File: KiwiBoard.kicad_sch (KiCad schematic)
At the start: 22 parts, among them J1 12V Power, J1 Motor Connector, J2 Heater, J3 Encoder Connector, J3 Expansion, J3 Fan, J4 OLED, K1 G5LE-14 DC3, Q1 PN2222A, Q3 TIP120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

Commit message: Change to JST PH connectors for OLED and Encoder.  Adjust spacing for the 3v3 regulator
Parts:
- J3: footprint Connector_PinSocket_2.54mm:PinSocket_1x05_P2.54mm_Vertical -> Connector_JST:JST_PH_B5B-PH-K_1x05_P2.00mm_Vertical
- J4: footprint Connector_JST:JST_SH_BM04B-SRSS-TB_1x04-1MP_P1.00mm_Vertical -> Connector_JST:JST_PH_B5B-PH-K_1x05_P2.00mm_Vertical
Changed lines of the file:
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@@
       (effects (font (size 1.27 1.27)) (justify left))
     )
-    (property "Footprint" "Connector_PinSocket_2.54mm:PinSocket_1x05_P2.54mm_Vertical" (at 236.855 93.345 0)
+    (property "Footprint" "Connector_JST:JST_PH_B5B-PH-K_1x05_P2.00mm_Vertical" (at 236.855 93.345 0)
       (effects (font (size 1.27 1.27)) hide)
     )
@@
       (effects (font (size 1.27 1.27)) (justify left))
     )
-    (property "Footprint" "Connector_JST:JST_SH_BM04B-SRSS-TB_1x04-1MP_P1.00mm_Vertical" (at 231.775 73.025 0)
-      (effects (font (size 1.27 1.27)) hide)
-    )
+    (property "Footprint" "Connector_JST:JST_PH_B5B-PH-K_1x05_P2.00mm_Vertical" (at 231.775 73.025 0)
+      (effects (font (size 1.27 1.27)) hide)
+    )

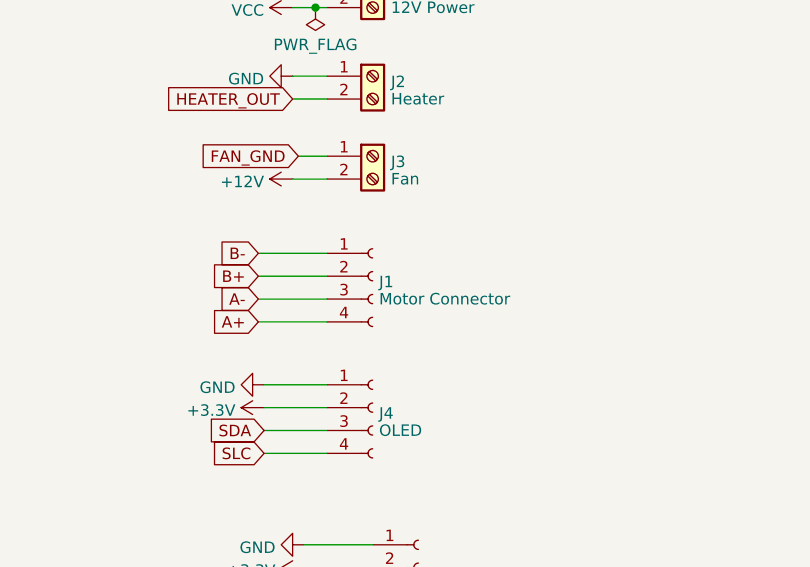
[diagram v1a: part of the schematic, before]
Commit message: Change to 2p connectors for the motor.  Retaining the ability to use the 2row connectors or one row connectors
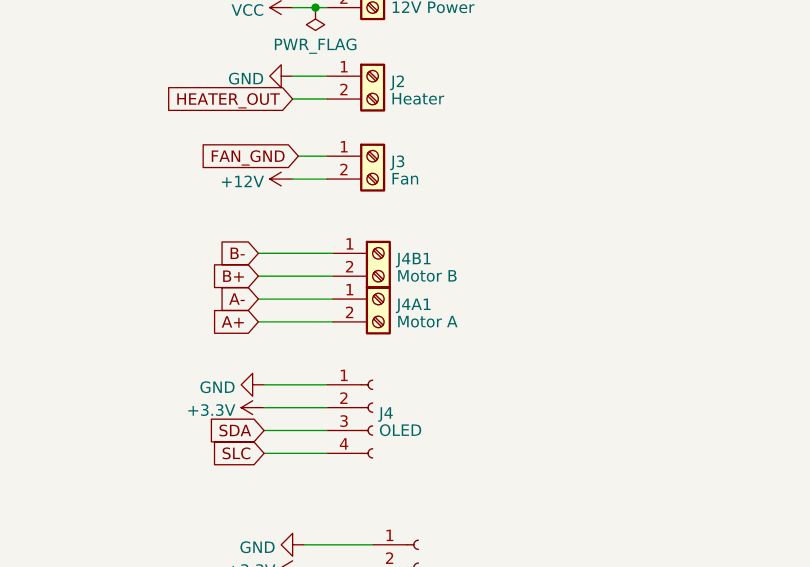
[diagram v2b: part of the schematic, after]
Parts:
- removed J1: Motor Connector, Library:PhoenixContact_LPT_2.5_4-H-5.0_1x04_P5.0mm_Horizontal, symbol Connector:Conn_01x04_Socket
- added J4A1: Motor A, Connector_Phoenix_SPT:PhoenixContact_SPT_2.5_2-H-5.0-EX_1x02_P5.0mm_Horizontal, symbol Connector:Screw_Terminal_01x02
- added J4B1: Motor B, Connector_Phoenix_SPT:PhoenixContact_SPT_2.5_2-H-5.0-EX_1x02_P5.0mm_Horizontal, symbol Connector:Screw_Terminal_01x02
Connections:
- net A+: now also J4A1.2 (Pin_2)
- net A-: now also J4A1.1 (Pin_1)
- net B+: now also J4B1.2 (Pin_2)
- net B-: now also J4B1.1 (Pin_1)
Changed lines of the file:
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@@
-    (stroke (width 0) (type default))
-  )
-  (wire (pts (xy 219.075 55.88) (xy 226.695 55.88))
     (stroke (width 0) (type default))
   )
@@
     (stroke (width 0) (type default))
   )
+  (wire (pts (xy 219.075 63.5) (xy 227.33 63.5))
+    (stroke (width 0) (type default))
+  )
   (wire (pts (xy 191.135 112.395) (xy 191.135 116.84))
     (stroke (width 0) (type default))
@@
     (stroke (width 0) (type default))
   )
+  (wire (pts (xy 219.075 60.96) (xy 227.33 60.96))
+    (stroke (width 0) (type default))
+  )
   (wire (pts (xy 41.91 114.935) (xy 50.8 114.935))
     (stroke (width 0) (type default))
@@
     (stroke (width 0) (type default))
   )
-  (wire (pts (xy 219.075 58.42) (xy 226.695 58.42))
+  (wire (pts (xy 219.075 55.88) (xy 227.33 55.88))
+    (stroke (width 0) (type default))
+  )
+  (wire (pts (xy 219.075 58.42) (xy 227.33 58.42))
     (stroke (width 0) (type default))
   )
@@
     (stroke (width 0) (type default))
   )
-  (wire (pts (xy 219.075 63.5) (xy 226.695 63.5))
-    (stroke (width 0) (type default))
-  )
   (wire (pts (xy 116.84 109.855) (xy 116.84 113.665))
     (stroke (width 0) (type default))
@@
   )
   (wire (pts (xy 226.06 114.935) (xy 233.045 114.935))
-    (stroke (width 0) (type default))
-  )
-  (wire (pts (xy 219.075 60.96) (xy 226.695 60.96))
     (stroke (width 0) (type default))
   )
@@
     )
   )
-  (symbol (lib_id "Connector:Conn_01x04_Socket") (at 231.775 58.42 0) (unit 1)
-    (in_bom yes) (on_board yes) (dnp no)
-    (property "Reference" "J1" (at 232.4862 59.055 0)
-      (effects (font (size 1.27 1.27)) (justify left))
-    )
-    (property "Value" "Motor Connector" (at 232.4862 60.9673 0)
-      (effects (font (size 1.27 1.27)) (justify left))
-    )
-    (property "Footprint" "Library:PhoenixContact_LPT_2.5_4-H-5.0_1x04_P5.0mm_Horizontal" (at 231.775 58.42 0)
-      (effects (font (size 1.27 1.27)) hide)
-    )
-    (property "Datasheet" "~" (at 231.775 58.42 0)
-      (effects (font (size 1.27 1.27)) hide)
-    )
-    (property "PN" "1190299" (at 231.775 58.42 0)
-      (effects (font (size 1.27 1.27)) hide)
-    )
-    (pin "1")
-    (pin "2")
-    (pin "3")
-    (pin "4")
-    (instances
-      (project "StepperDriver"
-        (path "/26ef1a70-c85a-4de1-ab17-46e65c4fb1e8"
-          (reference "J1") (unit 1)
-        )
-      )
-      (project "KiwiBoard"
-        (path "/9e2b85e7-5337-4458-814c-b9b7284580a9"
-          (reference "J4") (unit 1)
-        )
-      )
-    )
-  )
   (symbol (lib_id "power:VCC") (at 222.885 28.575 90) (unit 1)
     (in_bom yes) (on_board yes) (dnp no) (fields_autoplaced)
@@
     )
   )
+  (symbol (lib_id "Connector:Screw_Terminal_01x02") (at 232.41 60.96 0) (unit 1)
+    (in_bom yes) (on_board yes) (dnp no) (fields_autoplaced)
+    (property "Reference" "J4A1" (at 234.442 61.5863 0)
+      (effects (font (size 1.27 1.27)) (justify left))
+    )
+    (property "Value" "Motor A" (at 234.442 63.5073 0)
+      (effects (font (size 1.27 1.27)) (justify left))
+    )
+    (property "Footprint" "Connector_Phoenix_SPT:PhoenixContact_SPT_2.5_2-H-5.0-EX_1x02_P5.0mm_Horizontal" (at 232.41 60.96 0)
+      (effects (font (size 1.27 1.27)) hide)
+    )
+    (property "Datasheet" "~" (at 232.41 60.96 0)
+      (effects (font (size 1.27 1.27)) hide)
+    )
+    (property "Part_Number" "1190297" (at 232.41 60.96 0)
+      (effects (font (size 1.27 1.27)) hide)
+    )
+    (pin "1")
+    (pin "2")
+    (instances
+      (project "KiwiBoard"
+        (path "/9e2b85e7-5337-4458-814c-b9b7284580a9"
+          (reference "J4A1") (unit 1)
+        )
+      )
+    )
+  )
   (symbol (lib_id "Device:R_Small_US") (at 116.84 104.775 0) (unit 1)
     (in_bom yes) (on_board yes) (dnp no)
@@
         )
       )
+    )
+  )
+  (symbol (lib_id "Connector:Screw_Terminal_01x02") (at 232.41 55.88 0) (unit 1)
+    (in_bom yes) (on_board yes) (dnp no) (fields_autoplaced)
+    (property "Reference" "J4B1" (at 234.442 56.5063 0)
+      (effects (font (size 1.27 1.27)) (justify left))
+    )
+    (property "Value" "Motor B" (at 234.442 58.4273 0)
+      (effects (font (size 1.27 1.27)) (justify left))
+    )
+    (property "Footprint" "Connector_Phoenix_SPT:PhoenixContact_SPT_2.5_2-H-5.0-EX_1x02_P5.0mm_Horizontal" (at 232.41 55.88 0)
+      (effects (font (size 1.27 1.27)) hide)
+    )
+    (property "Datasheet" "~" (at 232.41 55.88 0)
+      (effects (font (size 1.27 1.27)) hide)
+    )
+    (property "Part_Number" "1190297" (at 232.41 55.88 0)
+      (effects (font (size 1.27 1.27)) hide)
+    )
+    (pin "1")
+    (pin "2")
+    (instances
+      (project "KiwiBoard"
+        (path "/9e2b85e7-5337-4458-814c-b9b7284580a9"
+          (reference "J4B1") (unit 1)
+        )
+      )

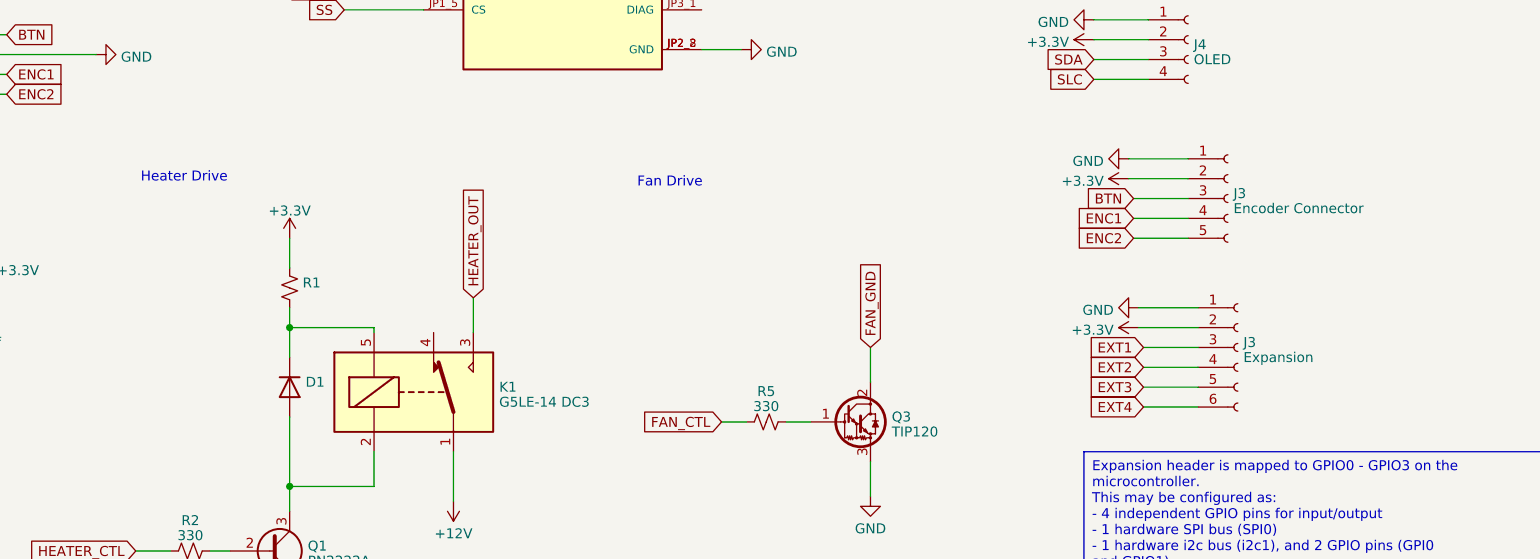
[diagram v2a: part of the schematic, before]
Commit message: reworked with JST PH connectors, move raspi to board edge
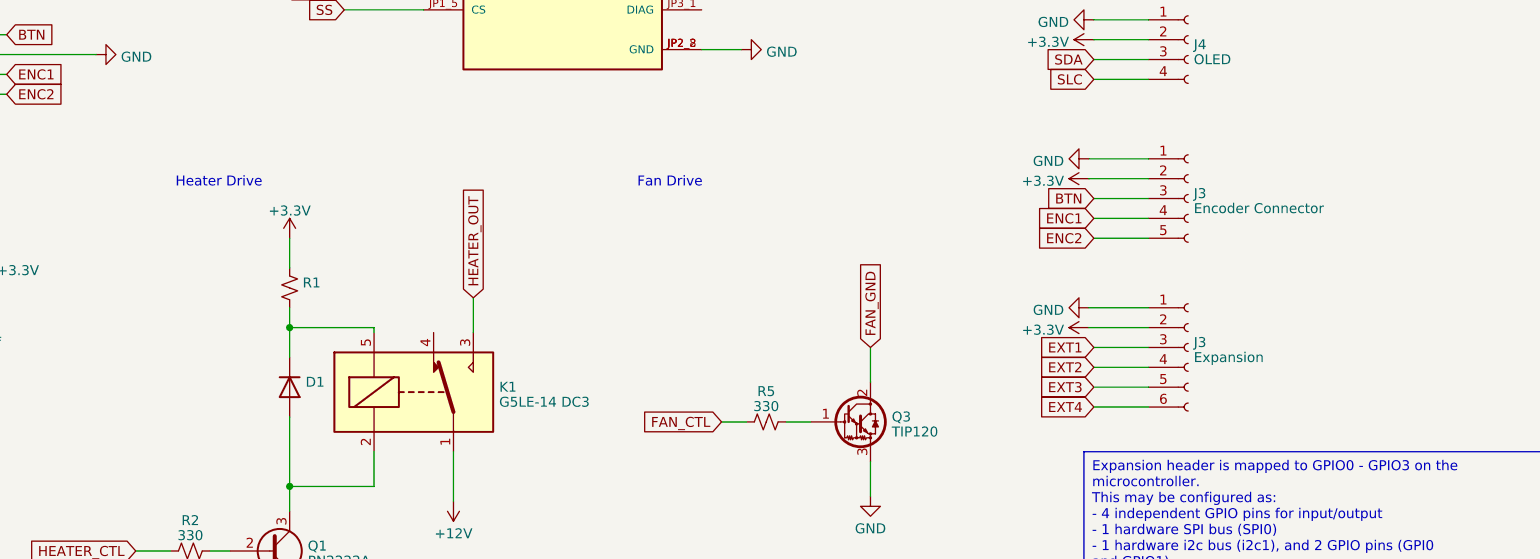
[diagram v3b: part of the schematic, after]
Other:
- moved on the sheet: J3

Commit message: Rev2 board, LCD connector, adjusted Q1 footprint.  Pico slid to edge
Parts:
- removed J4: OLED, Connector_JST:JST_PH_B5B-PH-K_1x05_P2.00mm_Vertical, symbol Connector:Conn_01x04_Socket
- added J4: LCD, Connector_JST:JST_PH_B9B-PH-K_1x09_P2.00mm_Vertical, symbol Connector:Conn_01x09_Socket
- Q1: footprint Package_TO_SOT_THT:TO-92_Inline -> Package_TO_SOT_THT:TO-92_HandSolder
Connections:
- net SDA is gone; now on net ENC2: U1.6 (GPIO4)
- net SLC is gone; now on net ENC1: U1.7 (GPIO5)
- net +3.3V: now also J4.1 (Pin_1)
- net BTN: now also U1.9 (GPIO6); no longer U1.24 (GPIO18)
- net ENC1: no longer U1.22 (GPIO17)
- net ENC2: no longer U1.21 (GPIO16)
- net GND: now also J4.2 (Pin_2)
- net LCD_MOSI: now reaches U1.25 (GPIO19)
- net LCD_MOSI: now also J4.6 (Pin_6)
- net LCD_CS: now reaches U1.26 (GPIO20)
- net LCD_CS: now also J4.3 (Pin_3)
- net LCD_DC: now reaches U1.27 (GPIO21)
- net LCD_DC: now also J4.5 (Pin_5)
- net LCD_RESET: now reaches U1.29 (GPIO22)
- net LCD_RESET: now also J4.4 (Pin_4)
- net LCD_BKLGHT: now reaches U1.31 (GPIO26_ADC0)
- net LCD_BKLGHT: now also J4.8 (Pin_8)
- new net LCD_MISO: J4.9 (Pin_9), U1.21 (GPIO16)
- new net LCD_SCK: J4.7 (Pin_7), U1.24 (GPIO18)
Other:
- note added: "V2-TFT"
- moved on the sheet: J3, U4
